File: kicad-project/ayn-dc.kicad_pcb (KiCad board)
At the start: 2 copper layers, 100 x 90 mm, 227 parts, among them J11 Conn_Coaxial, J12 Conn_Coaxial, J2 Si5351_Module, J3 BluePill_Left, J4 BluePill_Right, J5 Conn_01x03, J6 Conn_01x02, J8 Conn_Coaxial, J9 Conn_Coaxial, K1 G6K-2F-Y, K2 G6K-2F-Y, K3 G6K-2F-Y, K4 G6K-2F-Y, K5 G6K-2F-Y, K6 G6K-2F-Y, K7 G6K-2F-Y, K8 G6K-2F-Y, K9 G6K-2F-Y, Q1 MMBT3904, Q10 MMBT3904, Q11 MMBT3904, Q2 MMBF170, Q3 MMBF170, Q4 MMBT3906, Q5 MMBT3904, Q6 RD15HVF1, Q7 MMBT3904, Q8 MMBT3904, Q9 MMBT3904, T1 FT37-43, T10 T37-6, T11 T37-6, T2 FT37-43, T3 FT37-43, T4 T37-6, T5 T37-6, T6 T37-6, T7 T37-6, T8 T37-6, T9 T37-6, U1 L7805, U10 LM386, U2 24LC64, U3 NE5532, U4 FST3253, U5 74AC74, U6 NE5532, U7 NE5532, U8 NE5532, U9 NE5532

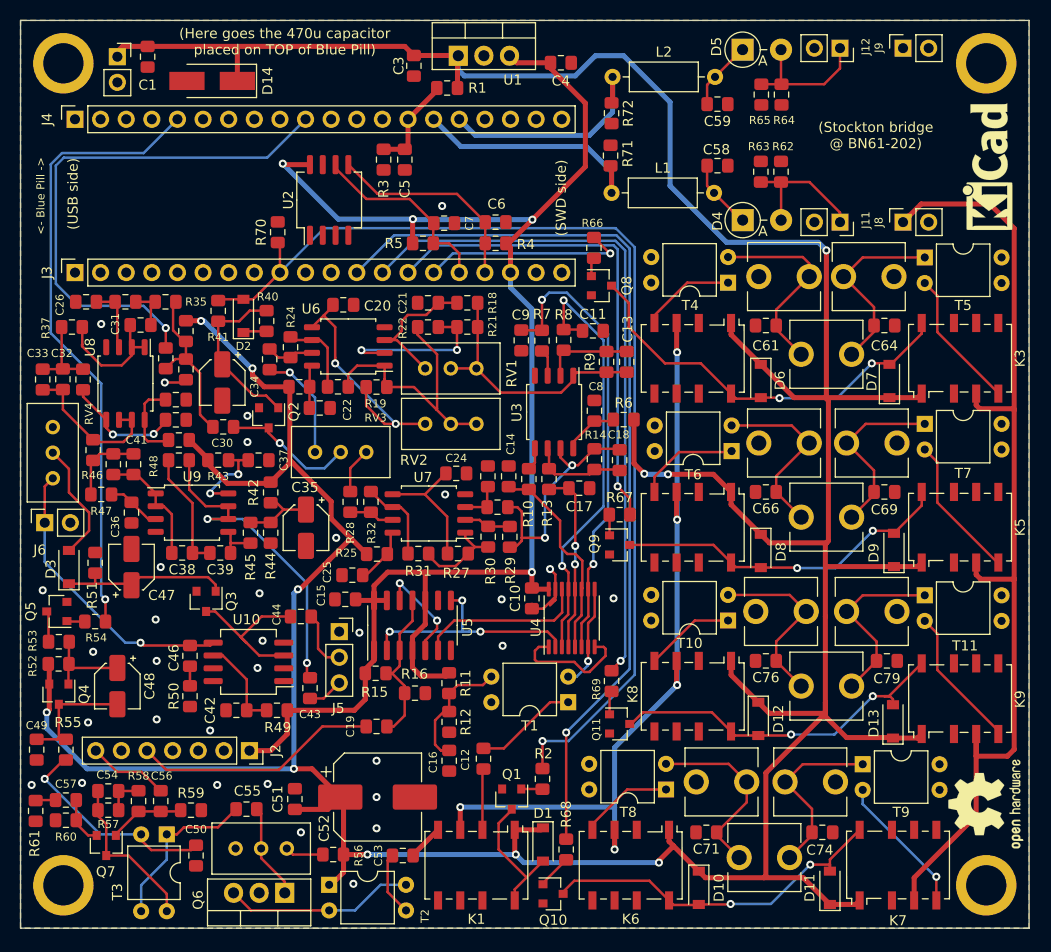
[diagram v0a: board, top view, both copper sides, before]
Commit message: Minor silkscreen + F_Fab layer fixes
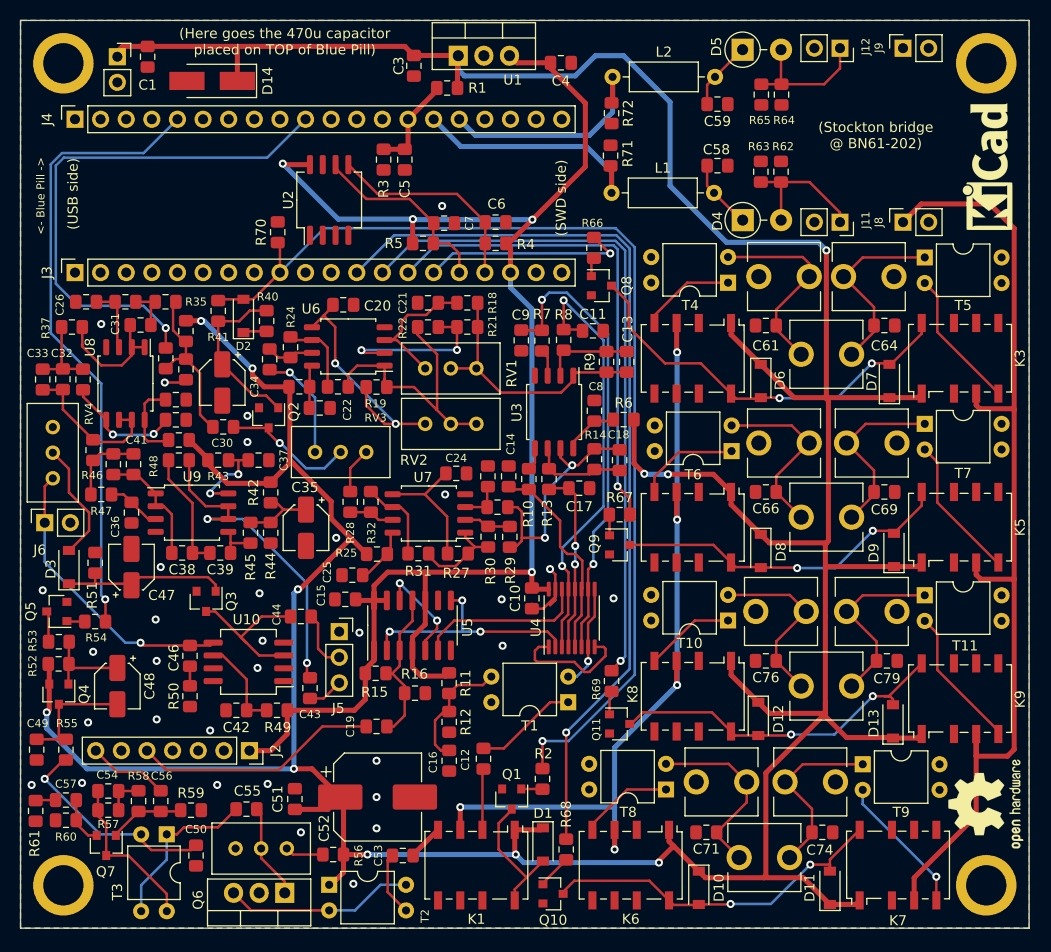
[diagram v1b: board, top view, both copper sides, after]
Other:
- board text added: "AYN/DC transceiver, PCB rev 2 Aleksander Alekseev, R2AUK, 2022 https://github.com/afiskon/ayn-dc"
- board text removed: "AYN/DC transceiver, PCB rev 2 Aleksander Alekseev, R2AUK, 2022 https://eax.me/ayn-dc-transceiver/"

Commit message: Add a bit more GND vias; update gerber.zip
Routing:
- net PWM_700HZ: track 53.1 -> 47.4 mm
- net SWR_BRIDGE: track 100.0 -> 101.5 mm
- net ENABLE_CW_TONE: track 62.0 -> 63.3 mm
- net AF_AMP_IN: track 6.75 -> 6.22 mm
- net GND: vias 32 -> 105

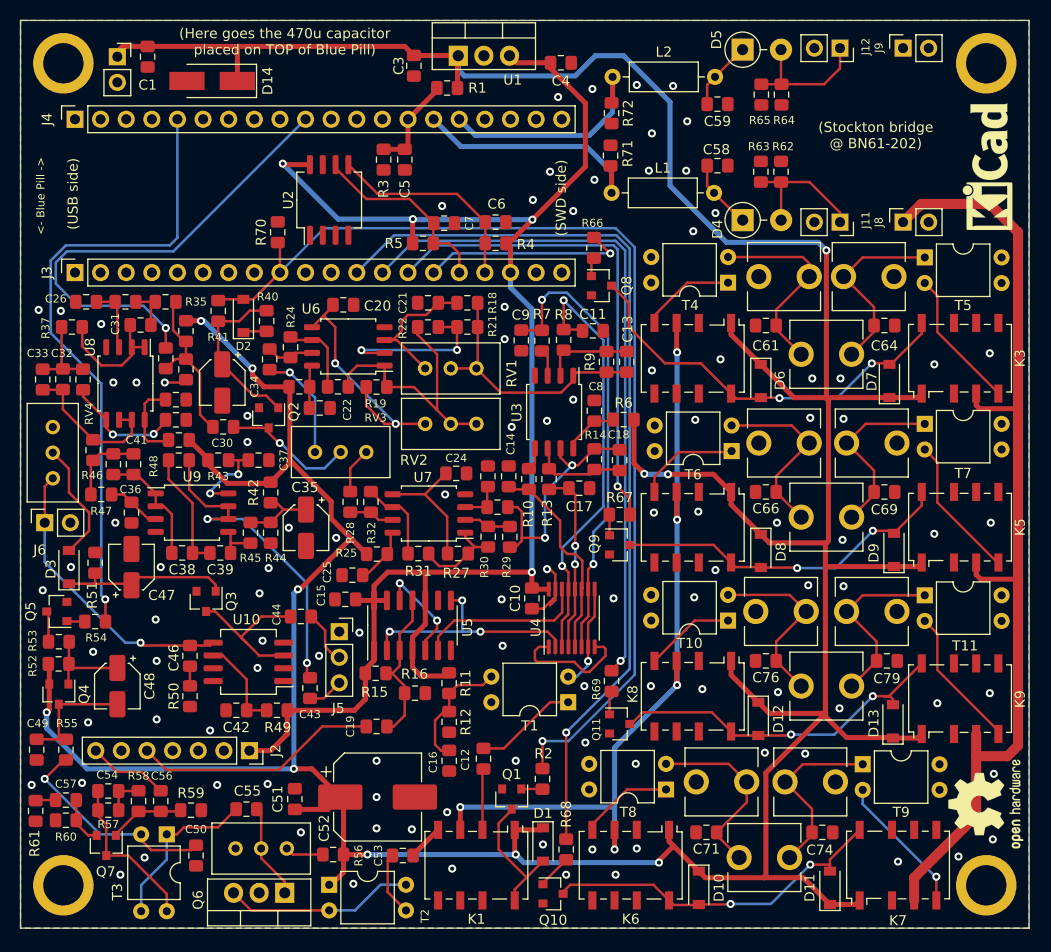
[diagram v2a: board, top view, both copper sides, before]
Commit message: HW: use 5V_DIGITAL and move I2C away from 5V bus
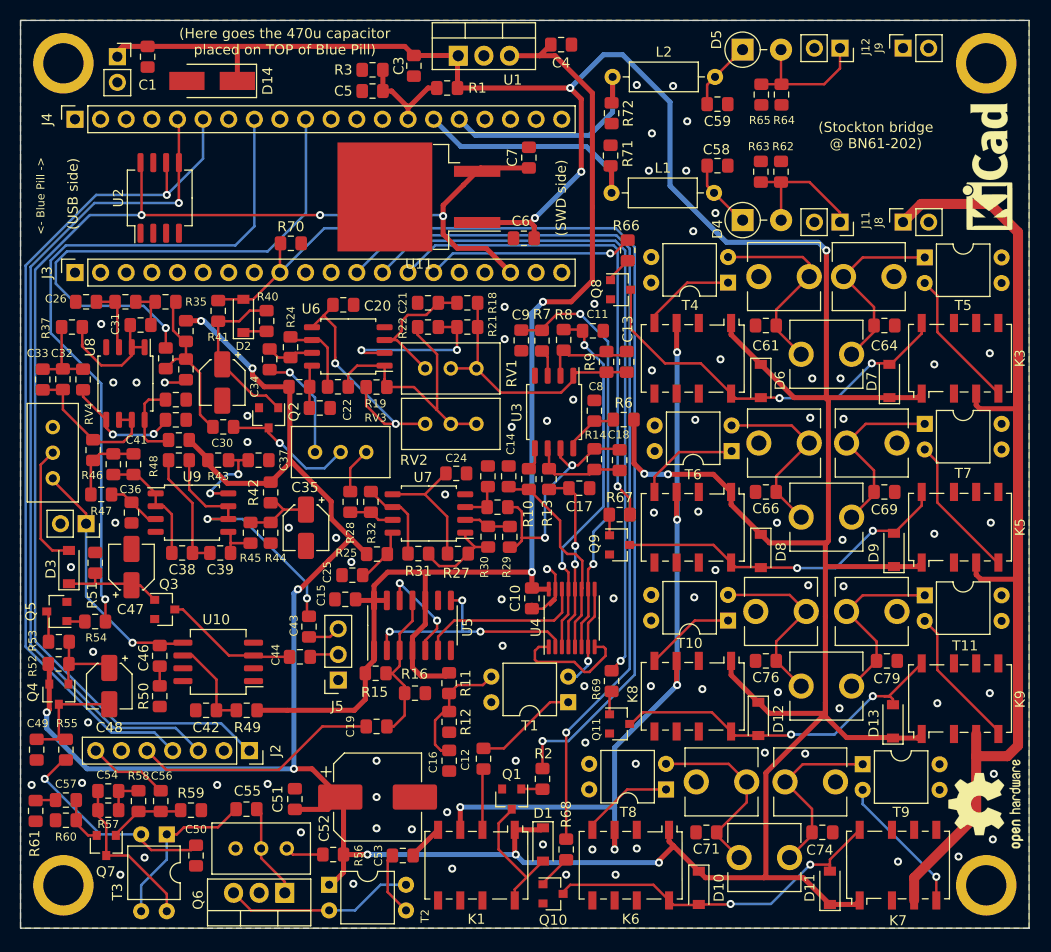
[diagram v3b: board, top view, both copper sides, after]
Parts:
- removed R4, R5: 4.7K, Resistor_SMD:R_0805_2012Metric_Pad1.15x1.40mm_HandSolder
- added U11: L7805, Package_TO_SOT_SMD:TO-263-2, F.Cu at (91.5, 54.5)
- C6: value DNP -> 0.47u
- C7: value DNP -> 0.1u
- moved U2 16.8 mm to (65.8, 54.6)
- moved C7 10.6 mm to (102.4, 50.6), turned to 90 degrees
- moved R3 8.97 mm to (86.9, 41.9), turned to 180 degrees
- moved C5 7.52 mm to (86.9, 44.0), turned to 180 degrees
- moved C43 6.10 mm to (80.6, 97.1)
- moved J5 4.80 mm to (83.5, 102.4), turned to 180 degrees
- moved Q3 4.18 mm to (66.3, 95.4), turned to 0 degrees
- moved J6 4.10 mm to (58.5, 86.9), turned to 270 degrees
- moved C44 4.00 mm to (79.7, 100.1)
- moved R66 3.36 mm to (112.2, 59.8)
- moved C6 3.22 mm to (101.9, 58.6), turned to 180 degrees
- moved C42 3.00 mm to (70.4, 105.4)
- moved C46 3.00 mm to (65.8, 100.0)
- moved R49 3.00 mm to (74.4, 105.4)
- moved R50 3.00 mm to (65.8, 104.0)
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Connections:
- net Net-(J3-Pad7) renamed LOCK_BTN_A10
- C6 pad 1: I2C_SDA -> +12V
- C7 pad 1: I2C_SCL -> 5V_DIGITAL
- J2 pad 1: +5V -> 5V_DIGITAL
- J2 pad 3: Net-(J2-Pad3) -> I2C_SDA
- J2 pad 4: Net-(J2-Pad4) -> I2C_SCL
- J3 pad 16: I2C_SCL -> Net-(J3-Pad16)
- J3 pad 17: I2C_SDA -> Net-(J3-Pad17)
- J3 pad 18: +5V -> 5V_DIGITAL
- J4 pad 5: ENABLE_CW_TONE -> I2C_SDA
- J4 pad 6: LOCK_BTN_B10 -> I2C_SCL
- J4 pad 8: Net-(J4-Pad8) -> ENABLE_CW_TONE
- U2 pad 8: +5V -> 5V_DIGITAL
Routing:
- net 5V_DIGITAL: track 0.00 -> 131.7 mm, vias 0 -> 3
- net I2C_SCL: track 19.3 -> 85.8 mm, vias 0 -> 1
- net I2C_SDA: track 20.9 -> 84.2 mm, vias 0 -> 1
- net +5V: track 156.3 -> 122.6 mm, vias 4 -> 2
- net +12V: track 429.6 -> 451.5 mm, vias 11 -> 14
- net ENABLE_CW_TONE: track 63.3 -> 70.3 mm
- net Net-(C47-Pad1): track 17.0 -> 10.2 mm
- net Net-(C11-Pad1): track 43.1 -> 36.4 mm
- net Net-(C43-Pad2): track 33.2 -> 26.7 mm
- net PWM_700HZ: track 47.4 -> 52.9 mm
- net Net-(C46-Pad1): track 28.9 -> 24.8 mm
- net Net-(C9-Pad1): track 45.8 -> 41.9 mm
- net Net-(C44-Pad1): track 16.6 -> 13.8 mm
- net AF_AMP_IN: track 6.22 -> 4.06 mm
- net GND40: track 40.6 -> 39.5 mm
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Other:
- board text added: "AYN/DC transceiver, PCB rev 3 Aleksander Alekseev, R2AUK, 2022 https://github.com/afiskon/ayn-dc"
- board text removed: "AYN/DC transceiver, PCB rev 2 Aleksander Alekseev, R2AUK, 2022 https://github.com/afiskon/ayn-dc"

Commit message: HW: minor changes
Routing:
- net GND: vias 86 -> 121
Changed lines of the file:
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@@
     (thickness 1.6)
     (drawings 12)
-    (tracks 1222)
+    (tracks 1256)
     (zones 0)
     (modules 226)
@@
     (tags "D2PAK DDPAK TO-263 D2PAK-3 TO-263-3 SOT-404")
     (attr smd)
-    (fp_text reference U11 (at 0 -6.65) (layer F.SilkS)
+    (fp_text reference U11 (at 9.4 0.1 90) (layer F.SilkS)
       (effects (font (size 1 1) (thickness 0.15)))
     )
@@
     (tags "SOIC SO")
     (attr smd)
-    (fp_text reference U9 (at 0 -3.56) (layer F.SilkS)
+    (fp_text reference U9 (at -0.7 -3.5) (layer F.SilkS)
       (effects (font (size 1 1) (thickness 0.15)))
     )
@@
     (descr "Potentiometer, vertical, Bourns 3296W, https://www.bourns.com/pdfs/3296.pdf")
     (tags "Potentiometer vertical Bourns 3296W")
-    (fp_text reference RV4 (at -6.4 -3.6 90) (layer F.SilkS)
+    (fp_text reference RV4 (at 3.2 1.8 180) (layer F.SilkS)
       (effects (font (size 0.8 0.8) (thickness 0.15)))
     )
@@
     (tags "resistor handsolder")
     (attr smd)
-    (fp_text reference R48 (at -2.5 0.6 90) (layer F.SilkS)
+    (fp_text reference R48 (at -2.5 0 270) (layer F.SilkS)
       (effects (font (size 0.8 0.8) (thickness 0.15)))
     )
@@
     (tags "resistor handsolder")
     (attr smd)
-    (fp_text reference R38 (at 0 -0.1 270) (layer F.SilkS) hide
+    (fp_text reference R38 (at -3.1 0.5 270) (layer F.SilkS)
       (effects (font (size 0.8 0.8) (thickness 0.15)))
     )
@@
     (tags SOT-23)
     (attr smd)
-    (fp_text reference Q4 (at -0.2 2.6 90) (layer F.SilkS)
+    (fp_text reference Q4 (at 0.3 2.6 90) (layer F.SilkS)
       (effects (font (size 1 1) (thickness 0.15)))
     )
@@
     (tags "capacitor handsolder")
     (attr smd)
-    (fp_text reference C41 (at -2.4 -0.3 180) (layer F.SilkS)
+    (fp_text reference C41 (at -2.5 0 180) (layer F.SilkS)
       (effects (font (size 0.8 0.8) (thickness 0.15)))
     )
@@
     (tags "capacitor handsolder")
     (attr smd)
-    (fp_text reference C27 (at 0 -1.65) (layer F.SilkS) hide
-      (effects (font (size 1 1) (thickness 0.15)))
+    (fp_text reference C27 (at 2.4 0.1 90) (layer F.SilkS)
+      (effects (font (size 0.8 0.8) (thickness 0.15)))
     )
     (fp_text value 1000p (at 0 1.65) (layer F.Fab) hide
@@
     (tags "capacitor handsolder")
     (attr smd)
-    (fp_text reference C20 (at 3.4 0.1) (layer F.SilkS)
+    (fp_text reference C20 (at 2.9 -0.1 90) (layer F.SilkS)
       (effects (font (size 1 1) (thickness 0.15)))
     )
@@
   (via (at 84.8 90.7) (size 0.8) (drill 0.4) (layers F.Cu B.Cu) (net 1))
   (via (at 108.9 65.1) (size 0.8) (drill 0.4) (layers F.Cu B.Cu) (net 1))
+  (via (at 76 91.9) (size 0.8) (drill 0.4) (layers F.Cu B.Cu) (net 1))
+  (via (at 77.4 103.4) (size 0.8) (drill 0.4) (layers F.Cu B.Cu) (net 1))
+  (via (at 80.9 103.5) (size 0.8) (drill 0.4) (layers F.Cu B.Cu) (net 1))
+  (via (at 77.4 106.8) (size 0.8) (drill 0.4) (layers F.Cu B.Cu) (net 1))
+  (via (at 80.7 106.7) (size 0.8) (drill 0.4) (layers F.Cu B.Cu) (net 1))
+  (via (at 85.6 97.7) (size 0.8) (drill 0.4) (layers F.Cu B.Cu) (net 1))
+  (via (at 85.7 99.8) (size 0.8) (drill 0.4) (layers F.Cu B.Cu) (net 1))
+  (via (at 71.3 100.6) (size 0.8) (drill 0.4) (layers F.Cu B.Cu) (net 1))
+  (via (at 71.2 93.9) (size 0.8) (drill 0.4) (layers F.Cu B.Cu) (net 1))
+  (via (at 75.8 96.2) (size 0.8) (drill 0.4) (layers F.Cu B.Cu) (net 1))
+  (via (at 67.7 105.2) (size 0.8) (drill 0.4) (layers F.Cu B.Cu) (net 1))
+  (via (at 63.4 105.7) (size 0.8) (drill 0.4) (layers F.Cu B.Cu) (net 1))
+  (via (at 61.3 98.8) (size 0.8) (drill 0.4) (layers F.Cu B.Cu) (net 1))
+  (via (at 63.5 96.5) (size 0.8) (drill 0.4) (layers F.Cu B.Cu) (net 1))
+  (via (at 58 95.1) (size 0.8) (drill 0.4) (layers F.Cu B.Cu) (net 1))
+  (via (at 55 93) (size 0.8) (drill 0.4) (layers F.Cu B.Cu) (net 1))
+  (via (at 53.2 102.6) (size 0.8) (drill 0.4) (layers F.Cu B.Cu) (net 1))
+  (via (at 56 65.7) (size 0.8) (drill 0.4) (layers F.Cu B.Cu) (net 1))
+  (via (at 66.3 49) (size 0.8) (drill 0.4) (layers F.Cu B.Cu) (net 1))
+  (via (at 68.9 49.1) (size 0.8) (drill 0.4) (layers F.Cu B.Cu) (net 1))
+  (via (at 91.4 38.4) (size 0.8) (drill 0.4) (layers F.Cu B.Cu) (net 1))
+  (via (at 82 41.8) (size 0.8) (drill 0.4) (layers F.Cu B.Cu) (net 1))
+  (via (at 77.6 41.8) (size 0.8) (drill 0.4) (layers F.Cu B.Cu) (net 1))
+  (via (at 66.8 41) (size 0.8) (drill 0.4) (layers F.Cu B.Cu) (net 1))
+  (via (at 60.9 38.4) (size 0.8) (drill 0.4) (layers F.Cu B.Cu) (net 1))
+  (via (at 94.2 50.1) (size 0.8) (drill 0.4) (layers F.Cu B.Cu) (net 1))
+  (via (at 82 50.2) (size 0.8) (drill 0.4) (layers F.Cu B.Cu) (net 1))
+  (via (at 97.3 54.6) (size 0.8) (drill 0.4) (layers F.Cu B.Cu) (net 1))
+  (via (at 103.7 53.2) (size 0.8) (drill 0.4) (layers F.Cu B.Cu) (net 1))
+  (via (at 107.1 55.5) (size 0.8) (drill 0.4) (layers F.Cu B.Cu) (net 1))
+  (via (at 110.5 56.2) (size 0.8) (drill 0.4) (layers F.Cu B.Cu) (net 1))
+  (via (at 107.5 61.8) (size 0.8) (drill 0.4) (layers F.Cu B.Cu) (net 1))
+  (via (at 102.3 103) (size 0.8) (drill 0.4) (layers F.Cu B.Cu) (net 1))
+  (via (at 80 77.8) (size 0.8) (drill 0.4) (layers F.Cu B.Cu) (net 1))
+  (via (at 82.7 77.8) (size 0.8) (drill 0.4) (layers F.Cu B.Cu) (net 1))
   (via (at 116.2 82) (size 0.8) (drill 0.4) (layers F.Cu B.Cu) (net 2))
   (via (at 69.9 66.8) (size 0.8) (drill 0.4) (layers F.Cu B.Cu) (net 2))
@@
   (segment (start 66.4 67.5) (end 66.400004 67.499996) (width 0.25) (layer F.Cu) (net 31))
   (segment (start 66.4 69.475) (end 66.4 67.5) (width 0.25) (layer F.Cu) (net 31))
-  (segment (start 55.5 63.1) (end 57.7 65.3) (width 0.25) (layer B.Cu) (net 31))
-  (segment (start 64.200008 65.3) (end 66.400004 67.499996) (width 0.25) (layer B.Cu) (net 31))
-  (segment (start 55.5 61) (end 55.5 63.1) (width 0.25) (layer B.Cu) (net 31))
-  (segment (start 56.6 59.9) (end 55.5 61) (width 0.25) (layer B.Cu) (net 31))
-  (segment (start 57.7 65.3) (end 64.200008 65.3) (width 0.25) (layer B.Cu) (net 31))
+  (segment (start 79.4 57) (end 79.4 47.66) (width 0.25) (layer B.Cu) (net 31))
+  (segment (start 76.5 59.9) (end 79.4 57) (width 0.25) (layer B.Cu) (net 31))
+  (segment (start 55.5 63.1) (end 55.5 61) (width 0.25) (layer B.Cu) (net 31))
+  (segment (start 79.4 47.66) (end 80.26 46.8) (width 0.25) (layer B.Cu) (net 31))
+  (segment (start 57.7 65.3) (end 55.5 63.1) (width 0.25) (layer B.Cu) (net 31))
   (segment (start 56.6 59.9) (end 76.5 59.9) (width 0.25) (layer B.Cu) (net 31))
-  (segment (start 76.5 59.9) (end 80.3 56.1) (width 0.25) (layer B.Cu) (net 31))
-  (segment (start 80.3 46.84) (end 80.26 46.8) (width 0.25) (layer B.Cu) (net 31))
-  (segment (start 80.3 56.1) (end 80.3 46.84) (width 0.25) (layer B.Cu) (net 31))
+  (segment (start 55.5 61) (end 56.6 59.9) (width 0.25) (layer B.Cu) (net 31))
+  (segment (start 64.200008 65.3) (end 57.7 65.3) (width 0.25) (layer B.Cu) (net 31))
+  (segment (start 66.400004 67.499996) (end 64.200008 65.3) (width 0.25) (layer B.Cu) (net 31))
   (via (at 77.7 78.9) (size 0.8) (drill 0.4) (layers F.Cu B.Cu) (net 32))
   (segment (start 73.225 77.4) (end 73.125 77.3) (width 0.25) (layer F.Cu) (net 32))
@@
   (segment (start 64.000002 51.205002) (end 63.895 51.1) (width 0.25) (layer F.Cu) (net 163))
   (segment (start 64.000002 56.3) (end 64.000002 51.205002) (width 0.25) (layer F.Cu) (net 163))
-  (segment (start 64.000002 56.3) (end 81.7 56.3) (width 0.25) (layer F.Cu) (net 163))
-  (segment (start 81.7 56.3) (end 81.7 56.3) (width 0.25) (layer F.Cu) (net 163))
-  (via (at 81.7 56.3) (size 0.8) (drill 0.4) (layers F.Cu B.Cu) (net 163))
-  (segment (start 93.8 56.3) (end 93.9 56.4) (width 0.25) (layer B.Cu) (net 163))
-  (segment (start 81.7 56.3) (end 93.8 56.3) (width 0.25) (layer B.Cu) (net 163))
   (via (at 93.9 56.4) (size 0.8) (drill 0.4) (layers F.Cu B.Cu) (net 163))
+  (via (at 80.399996 56.3) (size 0.8) (drill 0.4) (layers F.Cu B.Cu) (net 163))
+  (segment (start 64.000002 56.3) (end 80.399996 56.3) (width 0.25) (layer F.Cu) (net 163))
+  (segment (start 93.9 56.4) (end 80.499996 56.4) (width 0.25) (layer B.Cu) (net 163))
+  (segment (start 80.499996 56.4) (end 80.399996 56.3) (width 0.25) (layer B.Cu) (net 163))
   (zone (net 1) (net_name GND) (layer F.Cu) (hatch edge 0.508)
     (connect_pads (clearance 0.508))
